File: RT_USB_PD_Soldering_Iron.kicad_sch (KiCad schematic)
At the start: 64 parts, among them J1 USB4105-GF-A, J2 35RASMT4BHNTRX, J3 Conn_02x03_Odd_Even, SW1 SW_Push, SW2 SW_Push, U1 SPX3819M5-L-3-3, U2 ECMF02-AMX6, U3 FUSB302BMPX, U4 STM32G431Kxxx, U5 TPS25982ONRGET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

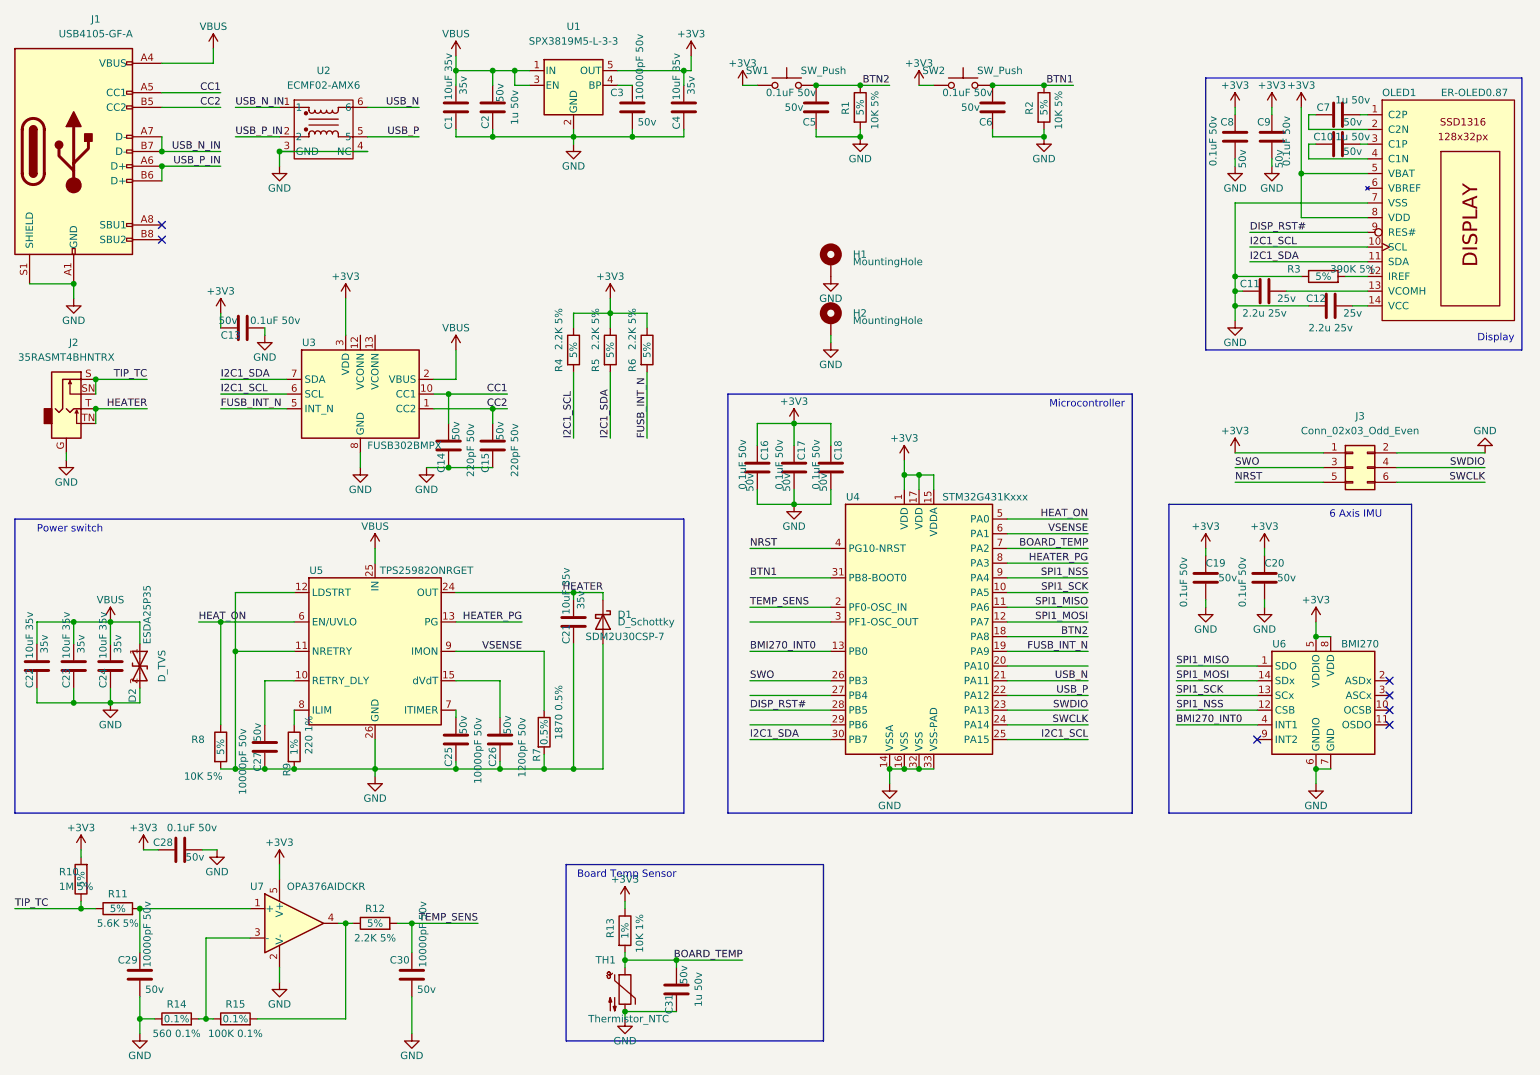
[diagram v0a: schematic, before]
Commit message: Update part values to part #
Update SW1, SW2, D1, D2 values to the part numbers
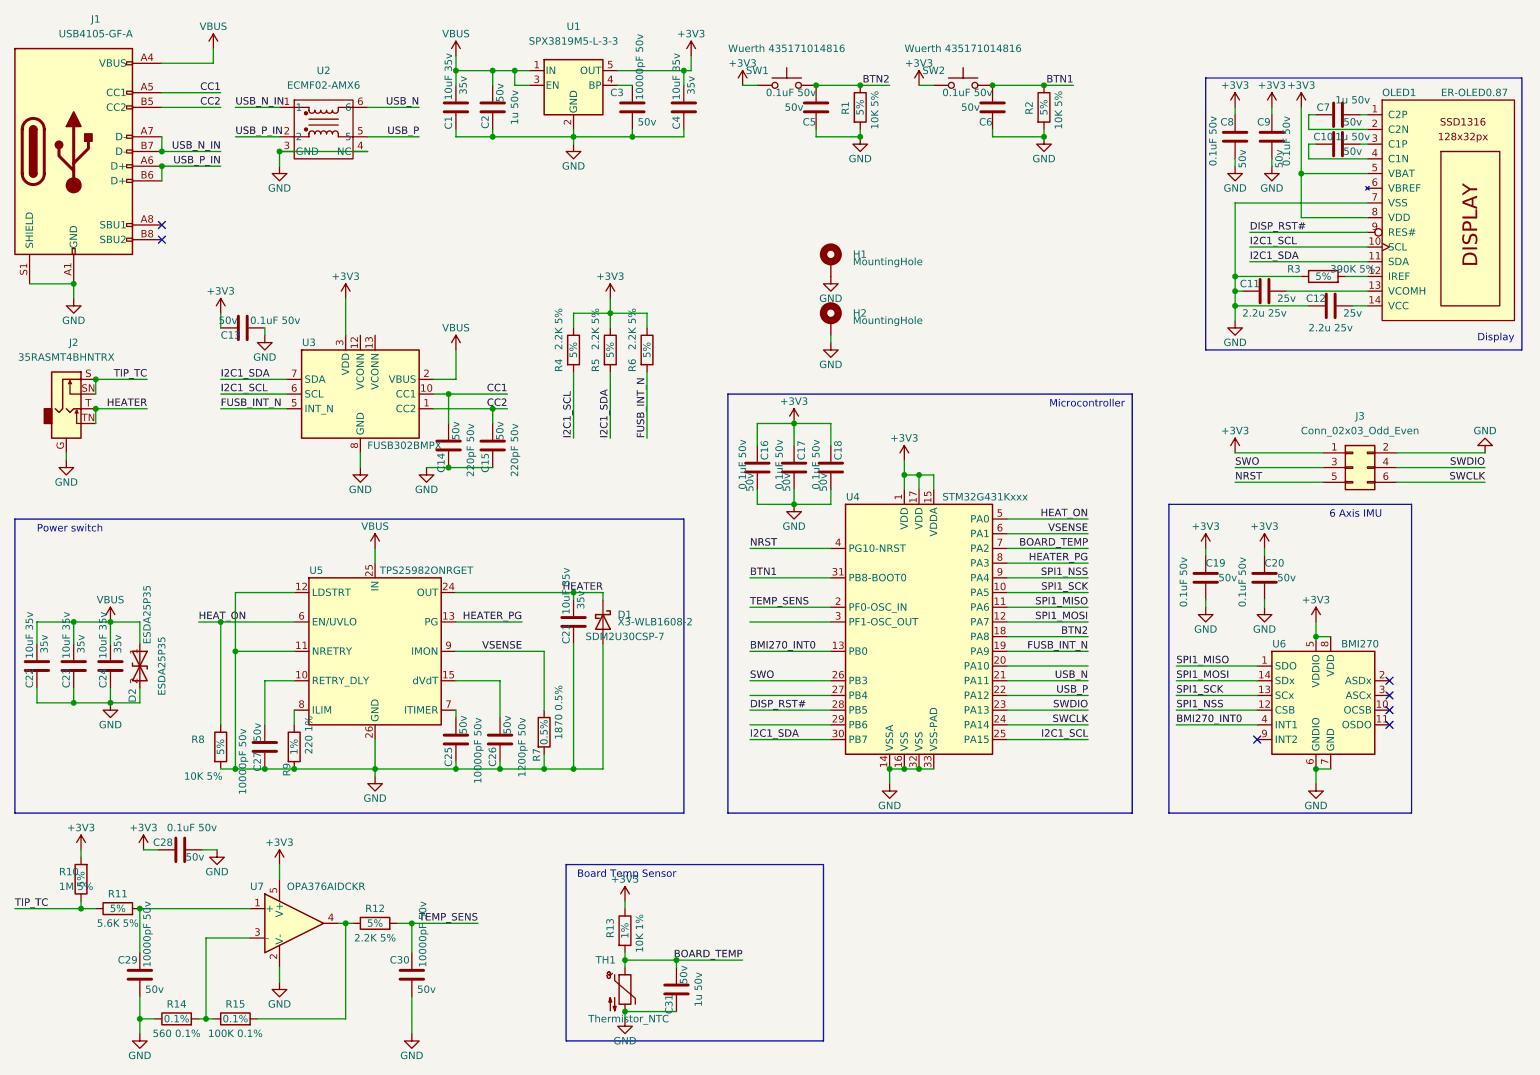
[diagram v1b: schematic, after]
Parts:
- D1: value D_Schottky -> X3-WLB1608-2
- D2: value D_TVS -> ESDA25P35
- SW1, SW2: value SW_Push -> Wuerth 435171014816; Part (none) -> Wuerth 435171014816
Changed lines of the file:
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@@
     (in_bom yes) (on_board yes)
     (property "Reference" "D2" (id 0) (at 38.1 132.08 0))
-    (property "Value" "D_TVS" (id 1) (at 43.18 127 0))
+    (property "Value" "ESDA25P35" (id 1) (at 43.18 127 0))
     (property "Footprint" "D_1610:D_1610" (id 2) (at 39.37 127 0)
       (effects (font (size 1.27 1.27)) hide)
@@
       (effects (font (size 1.27 1.27)) (justify left))
     )
-    (property "Value" "D_Schottky" (id 1) (at 121.92 119.38 90)
+    (property "Value" "X3-WLB1608-2" (id 1) (at 121.92 119.38 90)
       (effects (font (size 1.27 1.27)) (justify left))
     )
@@
     (in_bom yes) (on_board yes)
     (property "Reference" "SW1" (id 0) (at 146.05 24.13 0))
-    (property "Value" "SW_Push" (id 1) (at 157.48 24.13 0))
+    (property "Value" "Wuerth 435171014816" (id 1) (at 151.13 20.32 0))
     (property "Footprint" "Wurth:SW_Push_1P1T_NO_Vertical_Wuerth_434133025816" (id 2) (at 151.13 21.59 0)
       (effects (font (size 1.27 1.27)) hide)
@@
       (effects (font (size 1.27 1.27)) hide)
     )
+    (property "Part" "Wuerth 435171014816" (id 4) (at 151.13 26.67 0)
+      (effects (font (size 1.27 1.27)) hide)
+    )
     (pin "1")
     (pin "2")
@@
     (in_bom yes) (on_board yes)
     (property "Reference" "SW2" (id 0) (at 176.53 24.13 0))
-    (property "Value" "SW_Push" (id 1) (at 187.96 24.13 0))
+    (property "Value" "Wuerth 435171014816" (id 1) (at 181.61 20.32 0))
     (property "Footprint" "Wurth:SW_Push_1P1T_NO_Vertical_Wuerth_434133025816" (id 2) (at 181.61 21.59 0)
       (effects (font (size 1.27 1.27)) hide)
     )
     (property "Datasheet" "~" (id 3) (at 181.61 21.59 0)
+      (effects (font (size 1.27 1.27)) hide)
+    )
+    (property "Part" "Wuerth 435171014816" (id 4) (at 181.61 26.67 0)
       (effects (font (size 1.27 1.27)) hide)
     )
@@
     )
     (path "/df2137d6-6a3e-4b97-ae34-985653b3111b"
-      (reference "D1") (unit 1) (value "D_Schottky") (footprint "local:X3-WLB1608-2")
+      (reference "D1") (unit 1) (value "X3-WLB1608-2") (footprint "local:X3-WLB1608-2")
     )
     (path "/930b46a1-bcfa-4351-bda0-12fa566d3580"
-      (reference "D2") (unit 1) (value "D_TVS") (footprint "D_1610:D_1610")
+      (reference "D2") (unit 1) (value "ESDA25P35") (footprint "D_1610:D_1610")
     )
     (path "/ffc9b8c7-d039-4169-9ffd-a8a17d23ff13"
@@
     )
     (path "/139405bb-6375-4d55-8397-1248dc23e56b"
-      (reference "SW1") (unit 1) (value "SW_Push") (footprint "Wurth:SW_Push_1P1T_NO_Vertical_Wuerth_434133025816")
+      (reference "SW1") (unit 1) (value "Wuerth 435171014816") (footprint "Wurth:SW_Push_1P1T_NO_Vertical_Wuerth_434133025816")
     )
     (path "/f6a226e2-95e4-4448-86a4-9c284da06b8f"
-      (reference "SW2") (unit 1) (value "SW_Push") (footprint "Wurth:SW_Push_1P1T_NO_Vertical_Wuerth_434133025816")
+      (reference "SW2") (unit 1) (value "Wuerth 435171014816") (footprint "Wurth:SW_Push_1P1T_NO_Vertical_Wuerth_434133025816")
     )
     (path "/b1127f57-07b1-40d2-b827-d892a2ebad56"
